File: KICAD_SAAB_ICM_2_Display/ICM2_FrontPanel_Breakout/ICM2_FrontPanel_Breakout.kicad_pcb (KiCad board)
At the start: 2 copper layers, 69.8 x 22.9 mm, 6 parts, among them J1 Controls_1_29, J2 Controls_Connector, J3 Controls_2_30, J4 Display_Connector, J5 Conn_01x10, J6 Conn_01x10

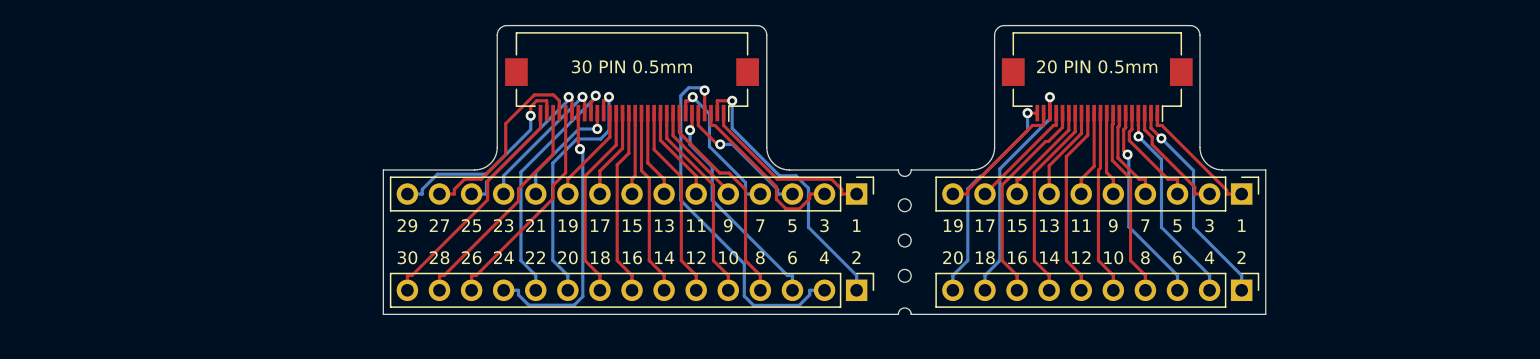
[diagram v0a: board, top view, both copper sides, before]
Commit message: Further refined FFC breakout board, quite happy with this design.
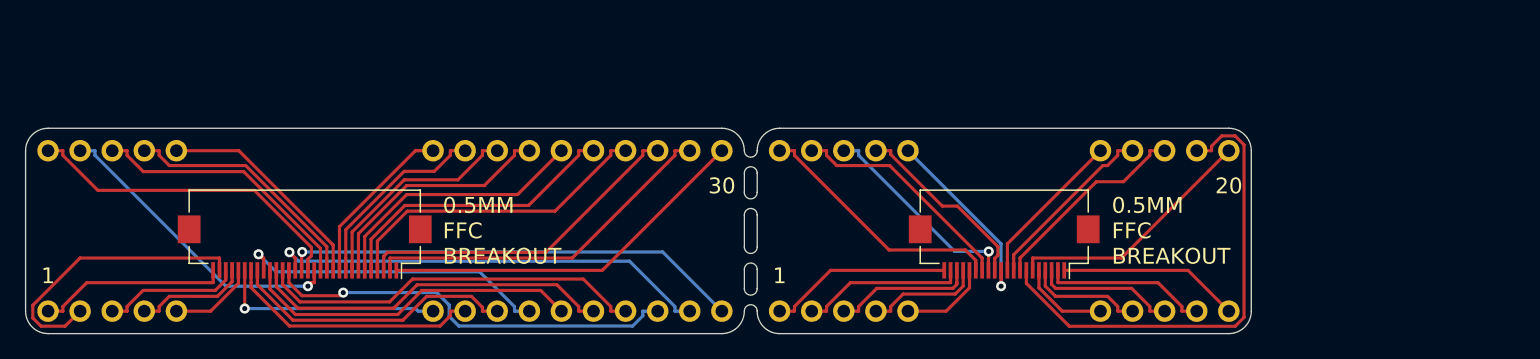
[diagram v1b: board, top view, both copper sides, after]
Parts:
- removed J3: Controls_2_30, Connector_PinHeader_2.54mm:PinHeader_1x15_P2.54mm_Vertical
- removed J4: Display_Connector, Connector_FFC-FPC:Hirose_FH12-20S-0.5SH_1x20-1MP_P0.50mm_Horizontal
- removed J5, J6: Conn_01x10, Connector_PinHeader_2.54mm:PinHeader_1x10_P2.54mm_Vertical
- added J1P1: P1-5, custom_symbols:PinHeader_1x05_P2.54mm_Vertical_Simple, F.Cu at (137.9, 74.7)
- added J1P10: P11-15, custom_symbols:PinHeader_1x05_P2.54mm_Vertical_Simple, F.Cu at (152.7, 74.7)
- added J1P2: P6-10, custom_symbols:PinHeader_1x05_P2.54mm_Vertical_Simple, F.Cu at (125.2, 74.7)
- added J1P3: P11-15, custom_symbols:PinHeader_1x05_P2.54mm_Vertical_Simple, F.Cu at (94.7, 74.7)
- added J1P4: P21-30, custom_symbols:PinHeader_1x05_P2.54mm_Vertical_Simple, F.Cu at (94.7, 87.4)
- added J1P5: P21-25, custom_symbols:PinHeader_1x05_P2.54mm_Vertical_Simple, F.Cu at (125.2, 87.4)
- added J1P6: P16-20, custom_symbols:PinHeader_1x05_P2.54mm_Vertical_Simple, F.Cu at (137.9, 87.4)
- added J1P7: P1-5, custom_symbols:PinHeader_1x05_P2.54mm_Vertical_Simple, F.Cu at (178.1, 87.4)
- added J1P8: P6-10, custom_symbols:PinHeader_1x05_P2.54mm_Vertical_Simple, F.Cu at (178.1, 74.7)
- added J1P9: P16-20, custom_symbols:PinHeader_1x05_P2.54mm_Vertical_Simple, F.Cu at (152.7, 87.4)
- J1: value Controls_1_29 -> Controls_Connector; footprint Connector_PinHeader_2.54mm:PinHeader_1x15_P2.54mm_Vertical -> Connector_FFC-FPC:Hirose_FH12-30S-0.5SH_1x30-1MP_P0.50mm_Horizontal
- J2: value Controls_Connector -> Display_Connector; footprint Connector_FFC-FPC:Hirose_FH12-30S-0.5SH_1x30-1MP_P0.50mm_Horizontal -> Connector_FFC-FPC:Hirose_FH12-20S-0.5SH_1x20-1MP_P0.50mm_Horizontal
- moved J1 43.9 mm to (104.9, 82.3), turned to 180 degrees
- moved J2 32.0 mm to (160.3, 82.3)
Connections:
- J2 pad 1: Net-(J1-Pad1) -> Net-(J1P7-Pad1)
- J2 pad 11: Net-(J1-Pad6) -> Net-(J1P10-Pad1)
- J2 pad 13: Net-(J1-Pad7) -> Net-(J1P10-Pad3)
- J2 pad 15: Net-(J1-Pad8) -> Net-(J1P10-Pad5)
- J2 pad 17: Net-(J1-Pad9) -> Net-(J1P9-Pad2)
- J2 pad 19: Net-(J1-Pad10) -> Net-(J1P9-Pad4)
- J2 pad 3: Net-(J1-Pad2) -> Net-(J1P7-Pad3)
- J2 pad 5: Net-(J1-Pad3) -> Net-(J1P7-Pad5)
- J2 pad 7: Net-(J1-Pad4) -> Net-(J1P8-Pad2)
- J2 pad 9: Net-(J1-Pad5) -> Net-(J1P8-Pad4)
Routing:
- net Net-(J1P8-Pad2): track 0.00 -> 38.4 mm
- net Net-(J1-Pad16): track 0.00 -> 36.6 mm, vias 0 -> 1
- net Net-(J1-Pad17): track 0.00 -> 35.5 mm, vias 0 -> 1
- net Net-(J1-Pad18): track 0.00 -> 33.0 mm, vias 0 -> 1
- net Net-(J1-Pad19): track 0.00 -> 30.9 mm
- net Net-(J1-Pad20): track 0.00 -> 29.0 mm
- net Net-(J1-Pad21): track 0.00 -> 26.9 mm
- net Net-(J1-Pad22): track 0.00 -> 25.0 mm, vias 0 -> 1
- net Net-(J1-Pad29): track 0.00 -> 22.8 mm
- net Net-(J1-Pad23): track 0.00 -> 22.7 mm
- net Net-(J2-Pad24): track 21.9 -> 0.00 mm, vias 1 -> 0
- net Net-(J1-Pad24): track 0.00 -> 20.3 mm
- net Net-(J1P7-Pad4): track 29.3 -> 9.20 mm, vias 1 -> 0
- net Net-(J1P10-Pad5): track 0.00 -> 20.1 mm
- net Net-(J2-Pad22): track 19.9 -> 0.00 mm, vias 1 -> 0
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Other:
- board size 69.8 x 22.9 mm -> 97 x 16.3 mm
- rule via_min_size: 0.4 -> 0.3
- board text added: "0.5MM FFC BREAKOUT"
- board text removed: "10"
- board text removed: "11"
- board text removed: "12"
- board text removed: "13"
- board text removed: "14"
- board text removed: "15"
- board text removed: "16"
- board text removed: "17"
- board text removed: "18"
- board text removed: "19"
- board text removed: "2"
- board text removed: "20 PIN 0.5mm"
- board text removed: "21"
- board text removed: "22"
- board text removed: "23"
- board text removed: "24"
- board text removed: "25"
- board text removed: "26"
- board text removed: "27"
- board text removed: "28"
- board text removed: "29"
- board text removed: "3"
- board text removed: "30 PIN 0.5mm"
- board text removed: "4"
- board text removed: "5"
- board text removed: "6"
- board text removed: "7"
- board text removed: "8"
- board text removed: "9"

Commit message: Experimenting with alternate style breakout for FFC cables
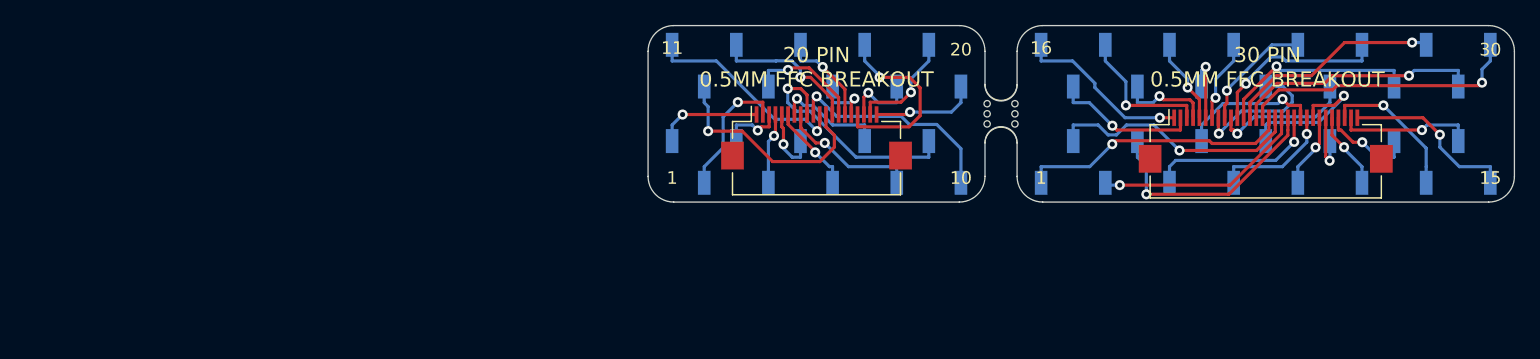
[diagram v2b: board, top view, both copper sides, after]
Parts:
- removed J1P1, J1P7: P1-5, custom_symbols:PinHeader_1x05_P2.54mm_Vertical_Simple
- removed J1P10, J1P3: P11-15, custom_symbols:PinHeader_1x05_P2.54mm_Vertical_Simple
- removed J1P2, J1P8: P6-10, custom_symbols:PinHeader_1x05_P2.54mm_Vertical_Simple
- removed J1P4: P21-30, custom_symbols:PinHeader_1x05_P2.54mm_Vertical_Simple
- removed J1P5: P21-25, custom_symbols:PinHeader_1x05_P2.54mm_Vertical_Simple
- removed J1P6, J1P9: P16-20, custom_symbols:PinHeader_1x05_P2.54mm_Vertical_Simple
- added J3: Conn_01x10, Connector_PinSocket_2.54mm:PinSocket_1x10_P2.54mm_Vertical_SMD_Pin1Left, B.Cu at (145.4, 67.9)
- added J4: Conn_01x15, Connector_PinSocket_2.54mm:PinSocket_1x15_P2.54mm_Vertical_SMD_Pin1Left, B.Cu at (181.0, 67.9)
- added J5: Conn_02x15_Odd_Even, Connector_FFC-FPC:Hirose_FH12-30S-0.5SH_1x30-1MP_P0.50mm_Horizontal, F.Cu at (181.0, 73.9)
- added J6: Conn_01x15, Connector_PinSocket_2.54mm:PinSocket_1x15_P2.54mm_Vertical_SMD_Pin1Left, B.Cu at (181.0, 75.6)
- added mouse-bite-2.54mm-slot: VAL**, custom_symbols:mouse-bite-2.54mm-slot, F.Cu at (160.0, 71.8)
- J1: value Controls_Connector -> Conn_01x10; footprint Connector_FFC-FPC:Hirose_FH12-30S-0.5SH_1x30-1MP_P0.50mm_Horizontal -> Connector_PinSocket_2.54mm:PinSocket_1x10_P2.54mm_Vertical_SMD_Pin1Left; moved to B.Cu
- J2: value Display_Connector -> Conn_02x10_Odd_Even
- moved J1 41.1 mm to (145.4, 75.6), turned to 270 degrees
- moved J2 17.2 mm to (145.4, 73.7), turned to 0 degrees
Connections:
- J2 pad 1: Net-(J1P7-Pad1) -> Net-(J1-Pad1)
- J2 pad 10: Net-(J1P8-Pad5) -> Net-(J1-Pad10)
- J2 pad 2: Net-(J1P7-Pad2) -> Net-(J1-Pad2)
- J2 pad 3: Net-(J1P7-Pad3) -> Net-(J1-Pad3)
- J2 pad 4: Net-(J1P7-Pad4) -> Net-(J1-Pad4)
- J2 pad 5: Net-(J1P7-Pad5) -> Net-(J1-Pad5)
- J2 pad 6: Net-(J1P8-Pad1) -> Net-(J1-Pad6)
- J2 pad 7: Net-(J1P8-Pad2) -> Net-(J1-Pad7)
- J2 pad 8: Net-(J1P8-Pad3) -> Net-(J1-Pad8)
- J2 pad 9: Net-(J1P8-Pad4) -> Net-(J1-Pad9)
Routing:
- net Net-(J1P8-Pad2): track 38.4 -> 0.00 mm
- net Net-(J1-Pad16): track 36.6 -> 0.00 mm, vias 1 -> 0
- net Net-(J1-Pad17): track 35.5 -> 0.00 mm, vias 1 -> 0
- net Net-(J1-Pad18): track 33.0 -> 0.00 mm, vias 1 -> 0
- net Net-(J1-Pad19): track 30.9 -> 0.00 mm
- net Net-(J1-Pad20): track 29.0 -> 0.00 mm
- net Net-(J1-Pad21): track 26.9 -> 0.00 mm
- net Net-(J1-Pad15): track 26.2 -> 0.00 mm
- net Net-(J1-Pad22): track 25.0 -> 0.00 mm, vias 1 -> 0
- net Net-(J1-Pad14): track 24.3 -> 0.00 mm, vias 1 -> 0
- net Net-(J1-Pad29): track 22.8 -> 0.00 mm
- net Net-(J1-Pad23): track 22.7 -> 0.00 mm
- net Net-(J4-Pad15): track 0.00 -> 22.3 mm, vias 0 -> 1
- net Net-(J5-Pad16): track 0.00 -> 21.7 mm, vias 0 -> 1
- net Net-(J1-Pad13): track 21.6 -> 0.00 mm
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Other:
- board size 97 x 16.3 mm -> 68.6 x 14 mm
- board text added: "10"
- board text added: "11"
- board text added: "15"
- board text added: "16"
- board text added: "20 PIN 0.5MM FFC BREAKOUT"
- board text added: "30 PIN 0.5MM FFC BREAKOUT"
- board text removed: "0.5MM FFC BREAKOUT"
